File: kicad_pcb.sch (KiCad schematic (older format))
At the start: 166 parts, among them J1 USB_B_Mini, SW1 SW_Push, U1 ATmega32U4-AU, Y1 16Mhz

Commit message: Ordered all keyboard rows
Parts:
- MX31, MX32, MX33, MX34, MX35, MX36, MX37, MX38, MX39, MX40, MX41, MX42, MX43, MX44, MX45, MX46, MX47, MX48, MX49, MX50, MX51, MX52, MX53, MX54, MX55, MX56, MX57, MX58, MX59, MX60, MX61, MX62, MX63, MX64, MX65, MX66, MX67, MX68, MX69, MX70, MX71, MX72, MX73, MX74, MX75: footprint (none) -> MX_Alps_Hybrid:MXOnly-1U-NoLED

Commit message: Renamed all footprints except bottom row
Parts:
- removed D23, D38: D_Small, Diode_SMD:D_0805_2012Metric, symbol Device:D_Small
- removed MX23: Y, MX_Alps_Hybrid:MXOnly-1U-NoLED, symbol MX_Alps_Hybrids:MX-1U
- removed MX38: MX-1U, MX_Alps_Hybrid:MXOnly-1U-NoLED, symbol MX_Alps_Hybrids:MX-1U
- MX17: value TAB -> Q
- MX18: value Q -> W
- MX19: value W -> E
- MX20: value E -> R
- MX21: value R -> T
- MX22: value T -> [
- MX24: value U -> ]
- MX25: value I -> Y
- MX26: value O -> U
- MX27: value P -> I
- MX28: value [ -> O
- MX29: value ] -> P
- MX31: value MX-1U -> LAYER_UP
- MX32: value MX-1U -> A
- MX33: value MX-1U -> S
- MX34: value MX-1U -> D
- MX35: value MX-1U -> F
- MX36: value MX-1U -> G
- MX37: value MX-1U -> HOME
- MX39: value MX-1U -> PAGE UP
- MX40: value MX-1U -> H
- MX41: value MX-1U -> J
- MX42: value MX-1U -> K
- MX43: value MX-1U -> L
- MX44: value MX-1U -> SEMI COLON
- MX45: value MX-1U -> RETURN
- MX46: value MX-1U -> L SHIFT
- MX47: value MX-1U -> Z
- MX48: value MX-1U -> X
- MX49: value MX-1U -> C
- MX50: value MX-1U -> V
- MX51: value MX-1U -> B
- MX52: value MX-1U -> END
- MX53: value MX-1U -> DELETE
- MX54: value MX-1U -> PAGE DOWN
- MX55: value MX-1U -> N
- MX56: value MX-1U -> M
- MX57: value MX-1U -> COMMA
- MX58: value MX-1U -> FULL STOP

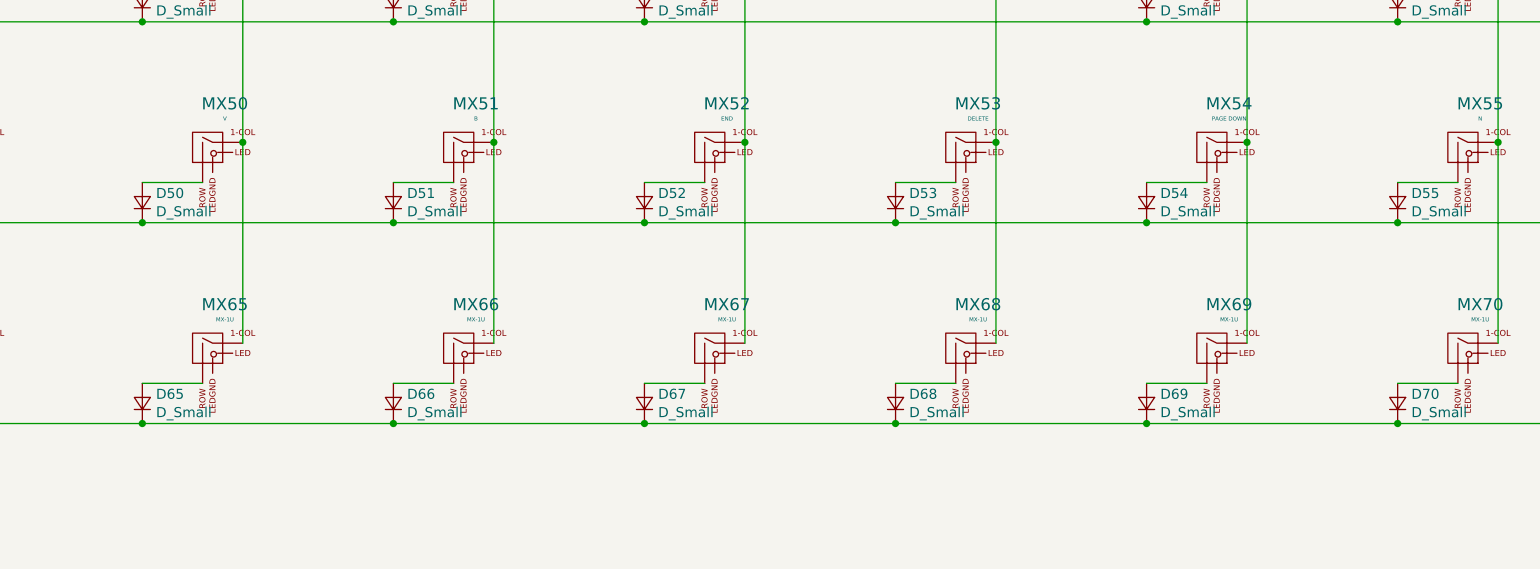
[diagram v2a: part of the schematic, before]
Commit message: placed all the diodes
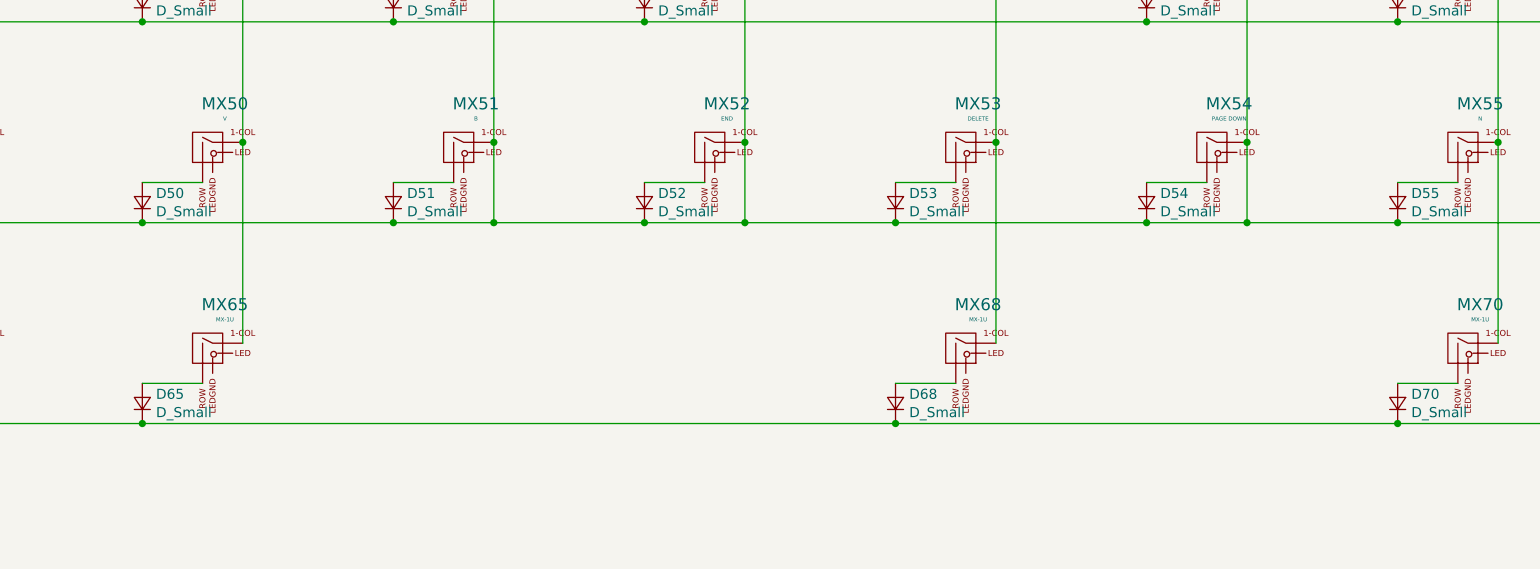
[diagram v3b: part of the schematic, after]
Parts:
- removed D66, D67, D69: D_Small, Diode_SMD:D_0805_2012Metric, symbol Device:D_Small
- removed MX66, MX67, MX69: MX-1U, MX_Alps_Hybrid:MXOnly-1U-NoLED, symbol MX_Alps_Hybrids:MX-1U
- MX62, MX63, MX64: footprint MX_Alps_Hybrid:MXOnly-1U-NoLED -> MX_Alps_Hybrid:MXOnly-1.25U-NoLED
- MX65: footprint MX_Alps_Hybrid:MXOnly-1U-NoLED -> MX_Alps_Hybrid:MXOnly-2.25U-NoLED
- MX70: footprint MX_Alps_Hybrid:MXOnly-1U-NoLED -> MX_Alps_Hybrid:MXOnly-2U-NoLED
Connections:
- net COL6 is gone; now on net COL5: MX22.1 (COL), MX37.1 (COL), MX52.1 (COL), MX7.1 (COL)
- net COL8 is gone; now on net COL5: MX24.1 (COL), MX39.1 (COL), MX54.1 (COL), MX9.1 (COL)
- net ROW3 is gone; now on net COL5: D46.1 (K), D47.1 (K), D48.1 (K), D49.1 (K), D50.1 (K), D51.1 (K), D52.1 (K), D53.1 (K), D54.1 (K), D55.1 (K), D56.1 (K), D57.1 (K), D58.1 (K), D59.1 (K), D60.1 (K)
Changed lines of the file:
@@
 	8750 6050 8750 5050
 Wire Wire Line
-	10000 5050 10000 6050
+	10000 5050 10000 5450
 Connection ~ 10000 5050
 Wire Wire Line
@@
 Connection ~ 11250 2050
 Wire Wire Line
-	11250 6050 11250 5050
+	11250 5450 11250 5050
 Wire Wire Line
 	12500 5050 12500 6050
@@
 Connection ~ 13750 2050
 Wire Wire Line
-	13750 6050 13750 5050
+	13750 5450 13750 5050
 Wire Wire Line
 	15000 5050 15000 6050
@@
 Connection ~ 14500 6450
 Connection ~ 12000 6450
-Wire Wire Line
-	10750 6450 12000 6450
-Connection ~ 10750 6450
-Wire Wire Line
-	9500 6450 10750 6450
-Connection ~ 9500 6450
-Wire Wire Line
-	8250 6450 9500 6450
 Connection ~ 8250 6450
 Wire Wire Line
@@
 Connection ~ 15750 5450
 Wire Wire Line
-	14500 5450 13250 5450
+	14500 5450 13750 5450
 Connection ~ 14500 5450
 Wire Wire Line
@@
 Connection ~ 13250 5450
 Wire Wire Line
-	12000 5450 10750 5450
+	12000 5450 11250 5450
 Connection ~ 12000 5450
 Wire Wire Line
-	10750 5450 9500 5450
+	10750 5450 10000 5450
 Connection ~ 10750 5450
 Wire Wire Line
@@
 F 0 "MX70" H 14911 6292 60  0000 C CNN
 F 1 "MX-1U" H 14911 6218 20  0000 C CNN
-F 2 "MX_Alps_Hybrid:MXOnly-1U-NoLED" H 14800 6050 60  0001 C CNN
+F 2 "MX_Alps_Hybrid:MXOnly-2U-NoLED" H 14800 6050 60  0001 C CNN
 F 3 "" H 14800 6050 60  0001 C CNN
 	1    14825 6075
@@
 	0    -1   -1   0
 $EndComp
-$Comp
-L Device:D_Small D67
-U 1 1 5D3EE66A
-P 10750 6350
-F 0 "D67" V 10796 6282 50  0000 R CNN
-F 1 "D_Small" V 10705 6282 50  0000 R CNN
-F 2 "Diode_SMD:D_0805_2012Metric" V 10750 6350 50  0001 C CNN
-F 3 "~" V 10750 6350 50  0001 C CNN
-	1    10750 6350
-	0    -1   -1   0
-$EndComp
 Wire Wire Line
 	10750 5250 11050 5250
@@
 $EndComp
 Wire Wire Line
-	9500 6250 9800 6250
-$Comp
-L MX_Alps_Hybrids:MX-1U MX66
-U 1 1 5D3EE6A5
-P 9825 6075
-F 0 "MX66" H 9911 6292 60  0000 C CNN
-F 1 "MX-1U" H 9911 6218 20  0000 C CNN
-F 2 "MX_Alps_Hybrid:MXOnly-1U-NoLED" H 9800 6050 60  0001 C CNN
-F 3 "" H 9800 6050 60  0001 C CNN
-	1    9825 6075
-	1    0    0    -1
-$EndComp
-$Comp
-L Device:D_Small D66
-U 1 1 5D3EE6AB
-P 9500 6350
-F 0 "D66" V 9546 6282 50  0000 R CNN
-F 1 "D_Small" V 9455 6282 50  0000 R CNN
-F 2 "Diode_SMD:D_0805_2012Metric" V 9500 6350 50  0001 C CNN
-F 3 "~" V 9500 6350 50  0001 C CNN
-	1    9500 6350
-	0    -1   -1   0
-$EndComp
-Wire Wire Line
 	9500 5250 9800 5250
 $Comp
@@
 F 0 "MX65" H 8661 6292 60  0000 C CNN
 F 1 "MX-1U" H 8661 6218 20  0000 C CNN
-F 2 "MX_Alps_Hybrid:MXOnly-1U-NoLED" H 8550 6050 60  0001 C CNN
+F 2 "MX_Alps_Hybrid:MXOnly-2.25U-NoLED" H 8550 6050 60  0001 C CNN
 F 3 "" H 8550 6050 60  0001 C CNN
 	1    8575 6075
@@
 F 0 "MX64" H 7411 6292 60  0000 C CNN
 F 1 "MX-1U" H 7411 6218 20  0000 C CNN
-F 2 "MX_Alps_Hybrid:MXOnly-1U-NoLED" H 7300 6050 60  0001 C CNN
+F 2 "MX_Alps_Hybrid:MXOnly-1.25U-NoLED" H 7300 6050 60  0001 C CNN
 F 3 "" H 7300 6050 60  0001 C CNN
 	1    7325 6075
@@
 F 0 "MX62" H 4836 6292 60  0000 C CNN
 F 1 "MX-1U" H 4836 6218 20  0000 C CNN
-F 2 "MX_Alps_Hybrid:MXOnly-1U-NoLED" H 4725 6050 60  0001 C CNN
+F 2 "MX_Alps_Hybrid:MXOnly-1.25U-NoLED" H 4725 6050 60  0001 C CNN
 F 3 "" H 4725 6050 60  0001 C CNN
 	1    4750 6075
@@
 F 0 "MX63" H 6161 6292 60  0000 C CNN
 F 1 "MX-1U" H 6161 6218 20  0000 C CNN
-F 2 "MX_Alps_Hybrid:MXOnly-1U-NoLED" H 6050 6050 60  0001 C CNN
+F 2 "MX_Alps_Hybrid:MXOnly-1.25U-NoLED" H 6050 6050 60  0001 C CNN
 F 3 "" H 6050 6050 60  0001 C CNN
 	1    6075 6075
@@
 Wire Wire Line
 	10750 4450 13250 4450
-Wire Wire Line
-	10750 6250 11050 6250
-$Comp
-L MX_Alps_Hybrids:MX-1U MX67
-U 1 1 5D3EE664
-P 11075 6075
-F 0 "MX67" H 11161 6292 60  0000 C CNN
-F 1 "MX-1U" H 11161 6218 20  0000 C CNN
-F 2 "MX_Alps_Hybrid:MXOnly-1U-NoLED" H 11050 6050 60  0001 C CNN
-F 3 "" H 11050 6050 60  0001 C CNN
-	1    11075 6075
-	1    0    0    -1
-$EndComp
-Wire Wire Line
-	12000 6450 13250 6450
-Wire Wire Line
-	13250 6450 14500 6450
-Connection ~ 13250 6450
-$Comp
-L Device:D_Small D69
-U 1 1 5D3EE5E8
-P 13250 6350
-F 0 "D69" V 13296 6282 50  0000 R CNN
-F 1 "D_Small" V 13205 6282 50  0000 R CNN
-F 2 "Diode_SMD:D_0805_2012Metric" V 13250 6350 50  0001 C CNN
-F 3 "~" V 13250 6350 50  0001 C CNN
-	1    13250 6350
-	0    -1   -1   0
-$EndComp
-Wire Wire Line
-	13250 6250 13550 6250
-$Comp
-L MX_Alps_Hybrids:MX-1U MX69
-U 1 1 5D3EE5E2
-P 13575 6075
-F 0 "MX69" H 13661 6292 60  0000 C CNN
-F 1 "MX-1U" H 13661 6218 20  0000 C CNN
-F 2 "MX_Alps_Hybrid:MXOnly-1U-NoLED" H 13550 6050 60  0001 C CNN
-F 3 "" H 13550 6050 60  0001 C CNN
-	1    13575 6075
-	1    0    0    -1
-$EndComp
 $Comp
 L MX_Alps_Hybrids:MX-1U MX60
@@
 	1    0    0    -1
 $EndComp
+Wire Wire Line
+	12000 6450 14500 6450
+Wire Wire Line
+	8250 6450 12000 6450
+Connection ~ 13750 5450
+Wire Wire Line
+	13750 5450 13250 5450
+Connection ~ 11250 5450
+Wire Wire Line
+	11250 5450 10750 5450
+Connection ~ 10000 5450
+Wire Wire Line
+	10000 5450 9500 5450
 $EndSCHEMATC

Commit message: updated the controller package
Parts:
- U1: footprint Package_QFP:TQFP-44_10x10mm_P0.8mm -> Package_QFP:TQFP-32_7x7mm_P0.8mm
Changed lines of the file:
@@
 F 0 "U1" H 8775 9911 50  0000 C CNN
 F 1 "ATmega32U4-AU" H 8775 9820 50  0000 C CNN
-F 2 "Package_QFP:TQFP-44_10x10mm_P0.8mm" H 8775 11800 50  0001 C CIN
+F 2 "Package_QFP:TQFP-32_7x7mm_P0.8mm" H 8775 11800 50  0001 C CIN
 F 3 "http://ww1.microchip.com/downloads/en/DeviceDoc/Atmel-7766-8-bit-AVR-ATmega16U4-32U4_Datasheet.pdf" H 8775 11800 50  0001 C CNN
 	1    8775 11800

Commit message: latest changes
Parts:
- added MX16-1: TAB, MX_Alps_Hybrid:MXOnly-1.5U-NoLED, symbol MX_Alps_Hybrids:MX-1U
- added MX30-1: BACKSPACE, MX_Alps_Hybrid:MXOnly-1.5U-NoLED, symbol MX_Alps_Hybrids:MX-1U
- added MX31-1: LAYER_UP, MX_Alps_Hybrid:MXOnly-1.25U-NoLED, symbol MX_Alps_Hybrids:MX-1U
- added MX37-1: HOME, MX_Alps_Hybrid:MXOnly-1.25U-NoLED, symbol MX_Alps_Hybrids:MX-1U
- added MX39-1: PAGE UP, MX_Alps_Hybrid:MXOnly-1.25U-NoLED, symbol MX_Alps_Hybrids:MX-1U
- added MX45-1: RETURN, MX_Alps_Hybrid:MXOnly-1.25U-NoLED, symbol MX_Alps_Hybrids:MX-1U
- MX16: value TAB -> TAB_orth
- MX30: value BACKSPACE -> BACKSPACE_orth
- MX31: value LAYER_UP -> LAYER_UP_orth
- MX37: value HOME -> HOME_orth
- MX39: value PAGE UP -> PAGE UP_orth
- MX45: value RETURN -> RETURN_orth
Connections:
- net COL0: now also MX16-1.1 (COL), MX31-1.1 (COL)
- net COL14: now also MX30-1.1 (COL), MX45-1.1 (COL)
- net COL5: now also MX37-1.1 (COL), MX39-1.1 (COL)
- net at D45.2 (A), MX45.2 (ROW): now also MX45-1.2 (ROW)
- net at D30.2 (A), MX30.2 (ROW): now also MX30-1.2 (ROW)
- net at D39.2 (A), MX39.2 (ROW): now also MX39-1.2 (ROW)
- net at D37.2 (A), MX37.2 (ROW): now also MX37-1.2 (ROW)
- net at D31.2 (A), MX31.2 (ROW): now also MX31-1.2 (ROW)
- net at D16.2 (A), MX16.2 (ROW): now also MX16-1.2 (ROW)
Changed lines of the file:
@@
 Connection ~ 11250 5050
 Wire Wire Line
-	11250 4050 11250 3050
+	11250 4050 11250 3800
 Connection ~ 11250 4050
 Connection ~ 11250 3050
@@
 Connection ~ 13750 5050
 Wire Wire Line
-	13750 4050 13750 3050
+	13750 4050 13750 3800
 Connection ~ 13750 4050
 Connection ~ 13750 3050
@@
 Connection ~ 21250 5050
 Wire Wire Line
-	21250 4050 21250 3050
+	21250 4050 21250 3800
 Connection ~ 21250 4050
 Connection ~ 21250 3050
@@
 P 21075 4075
 F 0 "MX45" H 21161 4292 60  0000 C CNN
-F 1 "RETURN" H 21161 4218 20  0000 C CNN
+F 1 "RETURN_orth" H 21161 4218 20  0000 C CNN
 F 2 "MX_Alps_Hybrid:MXOnly-1U-NoLED" H 21050 4050 60  0001 C CNN
 F 3 "" H 21050 4050 60  0001 C CNN
@@
 P 21075 3075
 F 0 "MX30" H 21161 3292 60  0000 C CNN
-F 1 "BACKSPACE" H 21161 3218 20  0000 C CNN
+F 1 "BACKSPACE_orth" H 21161 3218 20  0000 C CNN
 F 2 "MX_Alps_Hybrid:MXOnly-1U-NoLED" H 21050 3050 60  0001 C CNN
 F 3 "" H 21050 3050 60  0001 C CNN
@@
 P 13575 4075
 F 0 "MX39" H 13661 4292 60  0000 C CNN
-F 1 "PAGE UP" H 13661 4218 20  0000 C CNN
+F 1 "PAGE UP_orth" H 13661 4218 20  0000 C CNN
 F 2 "MX_Alps_Hybrid:MXOnly-1U-NoLED" H 13550 4050 60  0001 C CNN
 F 3 "" H 13550 4050 60  0001 C CNN
@@
 P 11075 4075
 F 0 "MX37" H 11161 4292 60  0000 C CNN
-F 1 "HOME" H 11161 4218 20  0000 C CNN
+F 1 "HOME_orth" H 11161 4218 20  0000 C CNN
 F 2 "MX_Alps_Hybrid:MXOnly-1U-NoLED" H 11050 4050 60  0001 C CNN
 F 3 "" H 11050 4050 60  0001 C CNN
@@
 P 3575 4075
 F 0 "MX31" H 3661 4292 60  0000 C CNN
-F 1 "LAYER_UP" H 3661 4218 20  0000 C CNN
+F 1 "LAYER_UP_orth" H 3661 4218 20  0000 C CNN
 F 2 "MX_Alps_Hybrid:MXOnly-1U-NoLED" H 3550 4050 60  0001 C CNN
 F 3 "" H 3550 4050 60  0001 C CNN
@@
 P 3575 3075
 F 0 "MX16" H 3661 3292 60  0000 C CNN
-F 1 "TAB" H 3661 3218 20  0000 C CNN
+F 1 "TAB_orth" H 3661 3218 20  0000 C CNN
 F 2 "MX_Alps_Hybrid:MXOnly-1U-NoLED" H 3550 3050 60  0001 C CNN
 F 3 "" H 3550 3050 60  0001 C CNN
@@
 Connection ~ 3750 2050
 Wire Wire Line
-	3750 3050 3750 2050
+	3750 3050 3750 2800
 Connection ~ 3750 3050
 Wire Wire Line
 	3750 5050 3750 4050
 Wire Wire Line
-	3750 4050 3750 3050
+	3750 4050 3750 3800
 Connection ~ 3750 4050
 Wire Wire Line
@@
 	18250 3250 18550 3250
 Wire Wire Line
-	21250 2050 21250 3050
+	21250 2050 21250 2800
 Wire Wire Line
 	20750 3250 21050 3250
@@
 Wire Wire Line
 	10000 5450 9500 5450
+$Comp
+L MX_Alps_Hybrids:MX-1U MX16-1
+U 1 1 5D209394
+P 3225 2825
+F 0 "MX16-1" H 3311 3042 60  0000 C CNN
+F 1 "TAB" H 3311 2968 20  0000 C CNN
+F 2 "MX_Alps_Hybrid:MXOnly-1.5U-NoLED" H 3200 2800 60  0001 C CNN
+F 3 "" H 3200 2800 60  0001 C CNN
+	1    3225 2825
+	1    0    0    -1
+$EndComp
+Wire Wire Line
+	3400 2800 3750 2800
+Connection ~ 3750 2800
+Wire Wire Line
+	3750 2800 3750 2050
+Wire Wire Line
+	3200 3000 3200 3250
+Wire Wire Line
+	3200 3250 3250 3250
+Connection ~ 3250 3250
+$Comp
+L MX_Alps_Hybrids:MX-1U MX31-1
+U 1 1 5D238BFB
+P 3250 3825
+F 0 "MX31-1" H 3336 4042 60  0000 C CNN
+F 1 "LAYER_UP" H 3336 3968 20  0000 C CNN
+F 2 "MX_Alps_Hybrid:MXOnly-1.25U-NoLED" H 3225 3800 60  0001 C CNN
+F 3 "" H 3225 3800 60  0001 C CNN
+	1    3250 3825
+	1    0    0    -1
+$EndComp
+Wire Wire Line
+	3425 3800 3750 3800
+Connection ~ 3750 3800
+Wire Wire Line
+	3750 3800 3750 3050
+Wire Wire Line
+	3225 4000 3225 4250
+Wire Wire Line
+	3225 4250 3250 4250
+Connection ~ 3250 4250
+$Comp
+L MX_Alps_Hybrids:MX-1U MX30-1
+U 1 1 5D268C5E
+P 20700 2825
+F 0 "MX30-1" H 20786 3042 60  0000 C CNN
+F 1 "BACKSPACE" H 20786 2968 20  0000 C CNN
+F 2 "MX_Alps_Hybrid:MXOnly-1.5U-NoLED" H 20675 2800 60  0001 C CNN
+F 3 "" H 20675 2800 60  0001 C CNN
+	1    20700 2825
+	1    0    0    -1
+$EndComp
+$Comp
+L MX_Alps_Hybrids:MX-1U MX45-1
+U 1 1 5D26AC7F
+P 20725 3825
+F 0 "MX45-1" H 20811 4042 60  0000 C CNN
+F 1 "RETURN" H 20811 3968 20  0000 C CNN
+F 2 "MX_Alps_Hybrid:MXOnly-1.25U-NoLED" H 20700 3800 60  0001 C CNN
+F 3 "" H 20700 3800 60  0001 C CNN
+	1    20725 3825
+	1    0    0    -1
+$EndComp
+Wire Wire Line
+	20900 3800 21250 3800
+Connection ~ 21250 3800
+Wire Wire Line
+	21250 3800 21250 3050
+Wire Wire Line
+	20700 4000 20700 4250
+Wire Wire Line
+	20700 4250 20750 4250
+Connection ~ 20750 4250
+Wire Wire Line
+	20675 3000 20675 3250
+Wire Wire Line
+	20675 3250 20750 3250
+Connection ~ 20750 3250
+Wire Wire Line
+	20875 2800 21250 2800
+Connection ~ 21250 2800
+Wire Wire Line
+	21250 2800 21250 3050
+$Comp
+L MX_Alps_Hybrids:MX-1U MX39-1
+U 1 1 5D2CCFFA
+P 13250 3825
+F 0 "MX39-1" H 13336 4042 60  0000 C CNN
+F 1 "PAGE UP" H 13336 3968 20  0000 C CNN
+F 2 "MX_Alps_Hybrid:MXOnly-1.25U-NoLED" H 13225 3800 60  0001 C CNN
+F 3 "" H 13225 3800 60  0001 C CNN
+	1    13250 3825
+	1    0    0    -1
+$EndComp
+$Comp
+L MX_Alps_Hybrids:MX-1U MX37-1
+U 1 1 5D2CD7EE
+P 10700 3825
+F 0 "MX37-1" H 10786 4042 60  0000 C CNN
+F 1 "HOME" H 10786 3968 20  0000 C CNN
+F 2 "MX_Alps_Hybrid:MXOnly-1.25U-NoLED" H 10675 3800 60  0001 C CNN
+F 3 "" H 10675 3800 60  0001 C CNN
+	1    10700 3825
+	1    0    0    -1
+$EndComp
+Wire Wire Line
+	10875 3800 11250 3800
+Connection ~ 11250 3800
+Wire Wire Line
+	11250 3800 11250 3050
+Wire Wire Line
+	10675 4000 10675 4250
+Wire Wire Line
+	10675 4250 10750 4250
+Connection ~ 10750 4250
+Wire Wire Line
+	13425 3800 13750 3800
+Connection ~ 13750 3800
+Wire Wire Line
+	13750 3800 13750 3050
+Wire Wire Line
+	13225 4000 13225 4250
+Wire Wire Line
+	13225 4250 13250 4250
+Connection ~ 13250 4250
 $EndSCHEMATC

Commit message: flipped each component to the correct side, placed everything
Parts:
- U1: footprint Package_QFP:TQFP-32_7x7mm_P0.8mm -> Package_QFP:TQFP-48_7x7mm_P0.5mm
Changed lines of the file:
@@
 F 0 "U1" H 8775 9911 50  0000 C CNN
 F 1 "ATmega32U4-AU" H 8775 9820 50  0000 C CNN
-F 2 "Package_QFP:TQFP-32_7x7mm_P0.8mm" H 8775 11800 50  0001 C CIN
+F 2 "Package_QFP:TQFP-48_7x7mm_P0.5mm" H 8775 11800 50  0001 C CIN
 F 3 "http://ww1.microchip.com/downloads/en/DeviceDoc/Atmel-7766-8-bit-AVR-ATmega16U4-32U4_Datasheet.pdf" H 8775 11800 50  0001 C CNN
 	1    8775 11800

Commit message: started with traces.
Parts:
- C1, C2, C3, C4, C5, C6: footprint Capacitor_SMD:C_0805_2012Metric -> Capacitor_SMD:C_0201_0603Metric
- F1: footprint Fuse:Fuse_1206_3216Metric -> Fuse:Fuse_0805_2012Metric
- R2, R3: footprint Resistor_SMD:R_0805_2012Metric -> Resistor_SMD:R_0603_1608Metric
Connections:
- net COL0: now also MX61.1 (COL)
- net COL1: now also MX62.1 (COL)
- net COL5: no longer D46.1 (K), D47.1 (K), D48.1 (K), D49.1 (K), D50.1 (K), D51.1 (K), D52.1 (K), D53.1 (K), D54.1 (K), D55.1 (K), D56.1 (K), D57.1 (K), D58.1 (K), D59.1 (K), D60.1 (K), MX22.1 (COL), MX24.1 (COL), MX37-1.1 (COL), MX37.1 (COL), MX39-1.1 (COL), MX39.1 (COL), MX52.1 (COL), MX54.1 (COL), MX7.1 (COL), MX9.1 (COL)
- new net COL6: MX22.1 (COL), MX37-1.1 (COL), MX37.1 (COL), MX52.1 (COL), MX7.1 (COL)
- new net COL8: MX24.1 (COL), MX39-1.1 (COL), MX39.1 (COL), MX54.1 (COL), MX9.1 (COL)
- new net ROW3: D46.1 (K), D47.1 (K), D48.1 (K), D49.1 (K), D50.1 (K), D51.1 (K), D52.1 (K), D53.1 (K), D54.1 (K), D55.1 (K), D56.1 (K), D57.1 (K), D58.1 (K), D59.1 (K), D60.1 (K)
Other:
- moved on the sheet: MX61, MX62

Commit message: further tracing
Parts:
- U1: footprint Package_QFP:TQFP-48_7x7mm_P0.5mm -> Package_QFP:TQFP-44_10x10mm_P0.8mm
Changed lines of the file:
@@
 F 0 "U1" H 8775 9911 50  0000 C CNN
 F 1 "ATmega32U4-AU" H 8775 9820 50  0000 C CNN
-F 2 "Package_QFP:TQFP-48_7x7mm_P0.5mm" H 8775 11800 50  0001 C CIN
+F 2 "Package_QFP:TQFP-44_10x10mm_P0.8mm" H 8775 11800 50  0001 C CIN
 F 3 "http://ww1.microchip.com/downloads/en/DeviceDoc/Atmel-7766-8-bit-AVR-ATmega16U4-32U4_Datasheet.pdf" H 8775 11800 50  0001 C CNN
 	1    8775 11800
